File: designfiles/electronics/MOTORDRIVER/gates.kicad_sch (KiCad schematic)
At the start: 39 parts, among them IC14 LM5109BSDX_NOPB, IC15 LM5109BSDX_NOPB, IC16 LM5109BSDX_NOPB, IC17 LM5109BSDX_NOPB, IC18 INA2181A2IDGSR, Q22 30V 71A, Q23 30V 71A, Q24 30V 71A, Q25 30V 71A, Q26 30V 71A, Q27 30V 71A, Q28 30V 71A

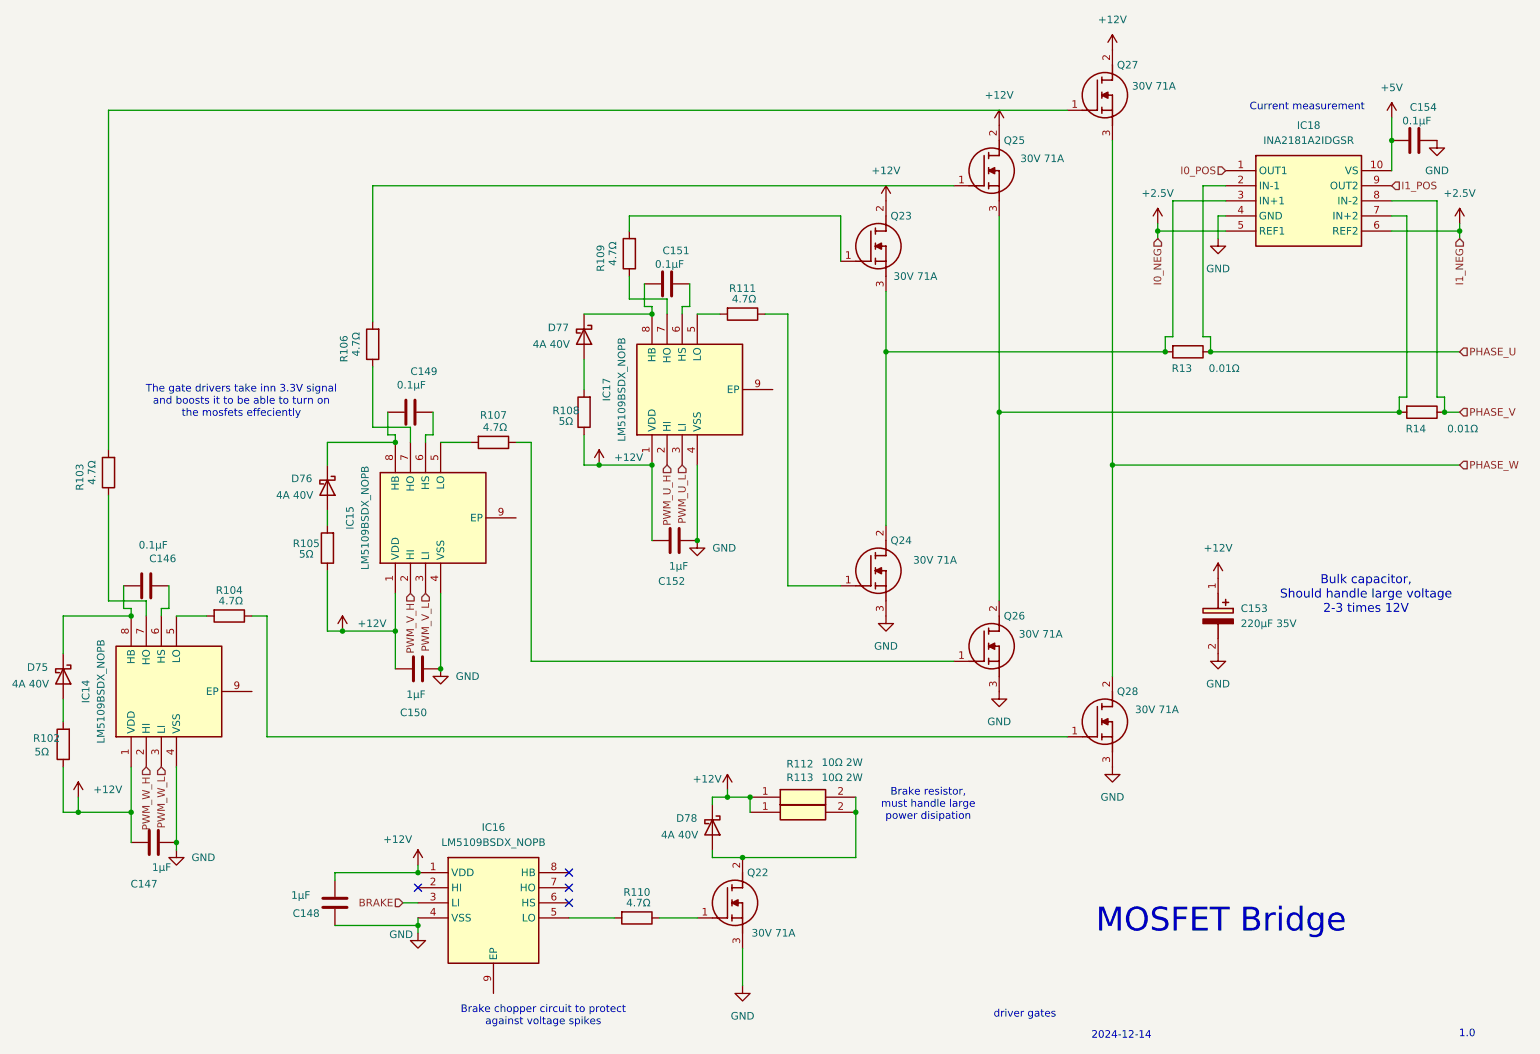
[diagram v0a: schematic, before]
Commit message: added design rules from pcbway, we need to redo some work to fit the design rules
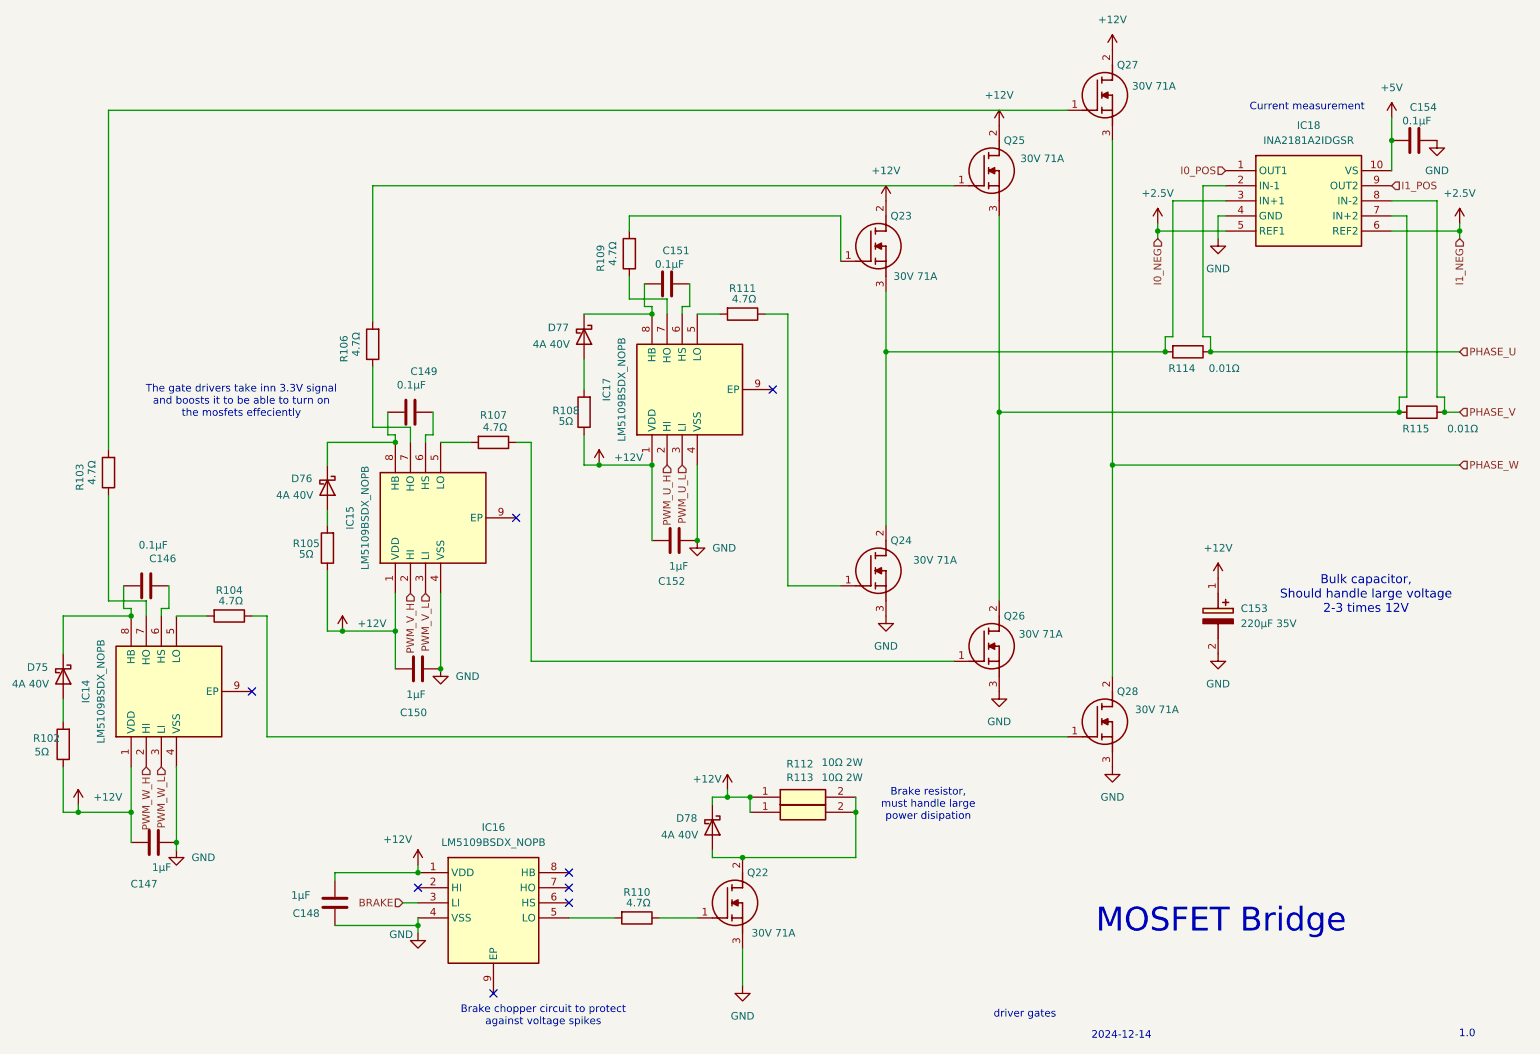
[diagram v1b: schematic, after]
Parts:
- renumbered R13 to R114, R14 to R115
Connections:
- no-connect marks 4 -> 8

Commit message: worked on pcb
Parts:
- renumbered C146 to C148, C147 to C149, C148 to C150, C149 to C151, C150 to C152, C151 to C153, C152 to C154, C153 to C155, C154 to C156
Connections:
- net +5V renamed +5VA
